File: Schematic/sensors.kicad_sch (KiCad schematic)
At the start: 19 parts, among them IC4 ICM-42688-P, IC5 MPU-6500, U4 QMC5883L, U5 SPL06-001

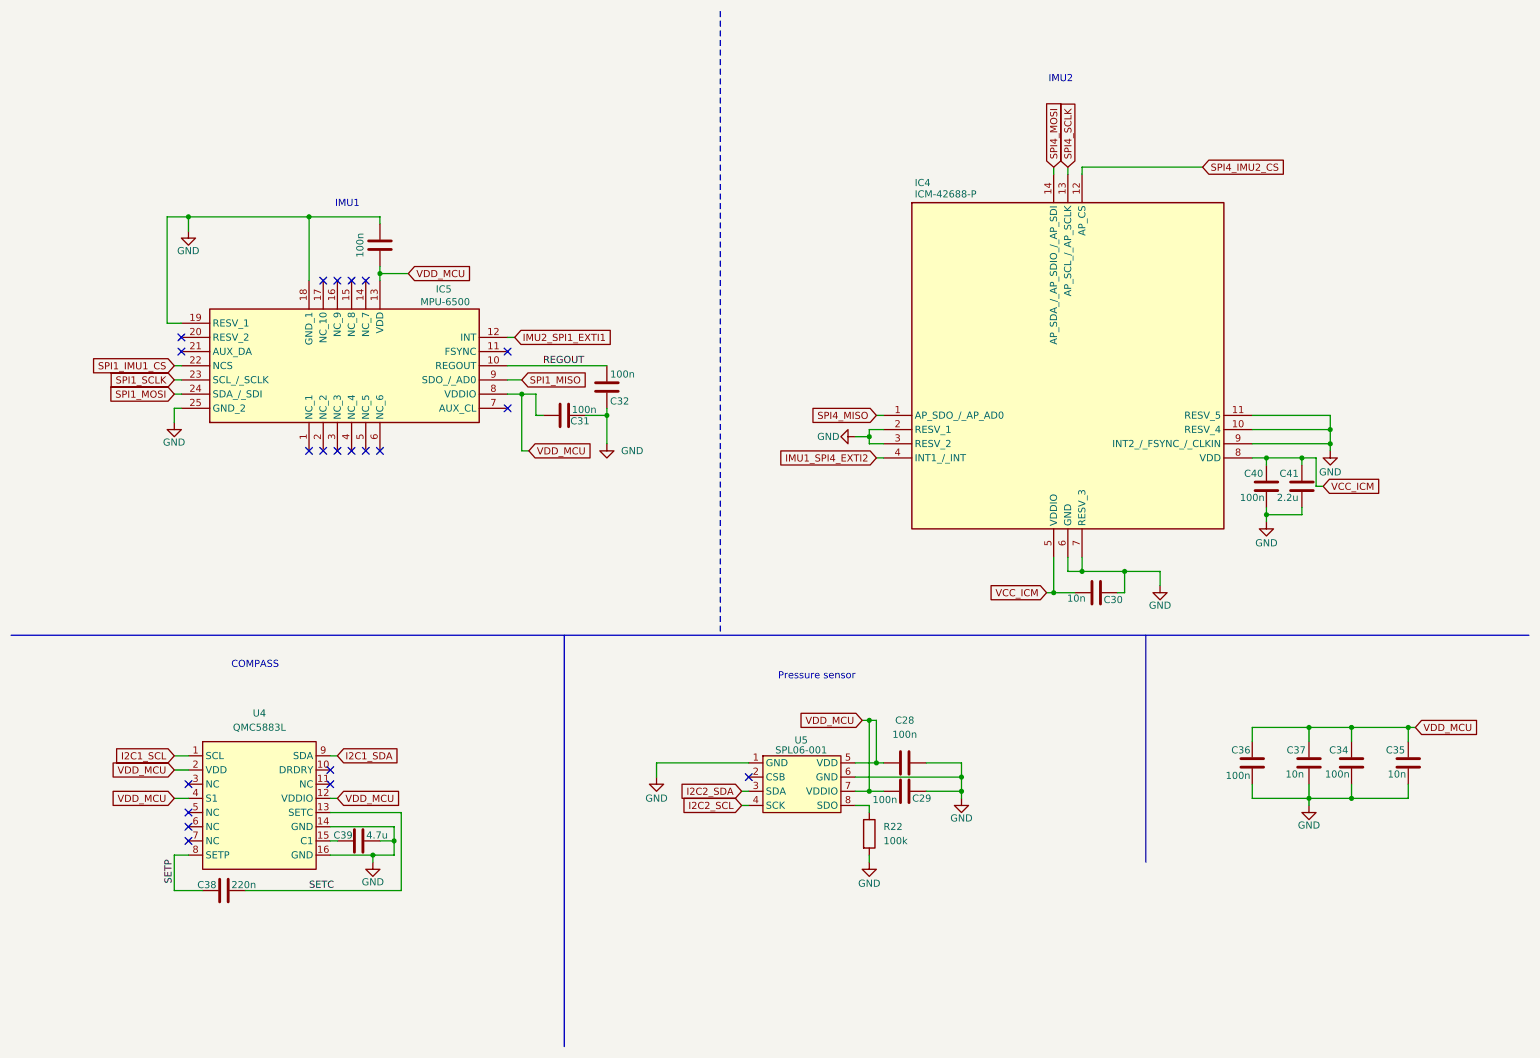
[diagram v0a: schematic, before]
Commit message: update: refine component labels for IMU and Magnetometer in schematic
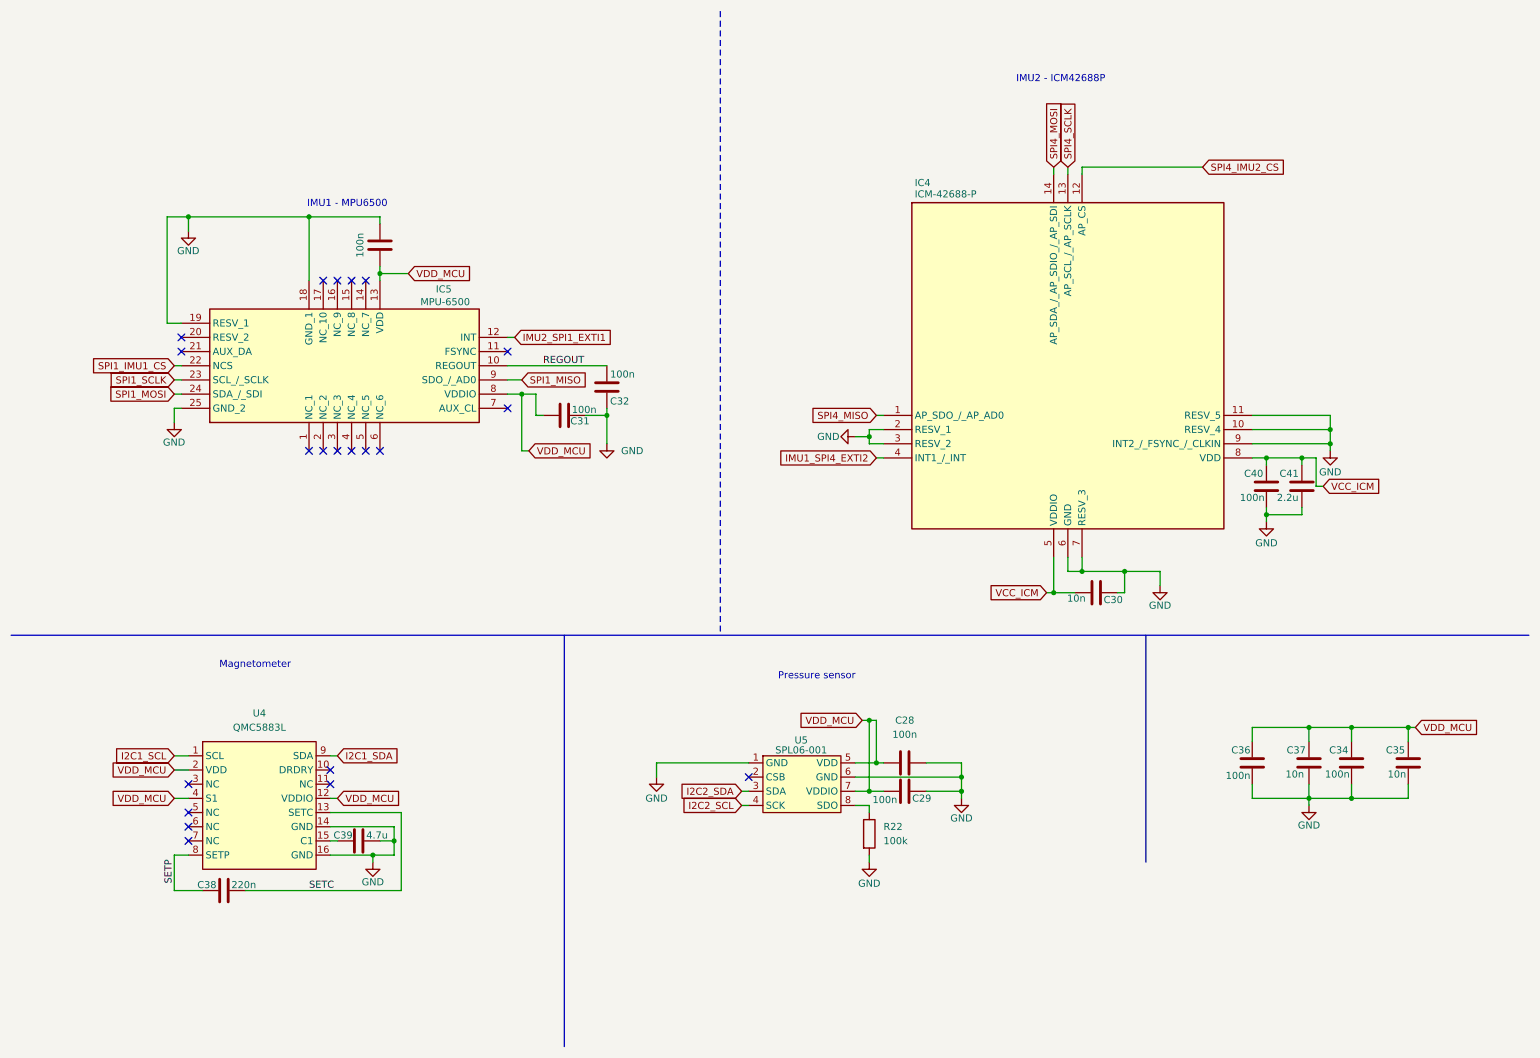
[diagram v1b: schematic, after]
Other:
- note added: "IMU1 - MPU6500"
- note added: "IMU2 - ICM42688P"
- note added: "Magnetometer"
- note removed: "COMPASS"
- note removed: "IMU1"
- note removed: "IMU2"
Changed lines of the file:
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@@
 	(generator_version "9.0")
 	(paper "A4")
-	(text "IMU2\n"
+	(text "IMU2 - ICM42688P\n"
 		(exclude_from_sim no)
 		(at 200.66 24.892 0)
@@
 		)
 	)
-	(text "IMU1\n"
+	(text "IMU1 - MPU6500\n"
 		(exclude_from_sim no)
 		(at 72.898 47.244 0)
@@
 		)
 	)
-	(text "COMPASS\n"
+	(text "Magnetometer\n"
 		(exclude_from_sim no)
 		(at 56.388 129.794 0)

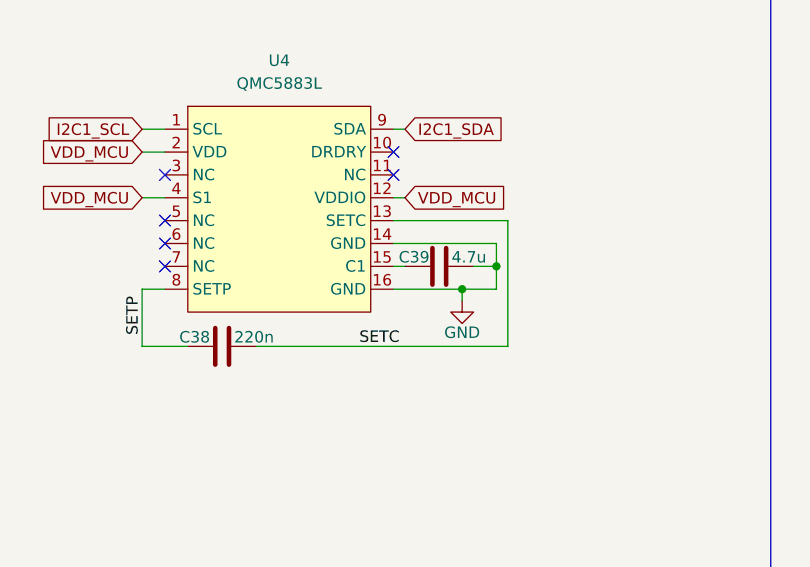
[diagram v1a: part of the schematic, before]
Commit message: Fix junction and wire positions in schematic; update capacitor and ground symbol properties
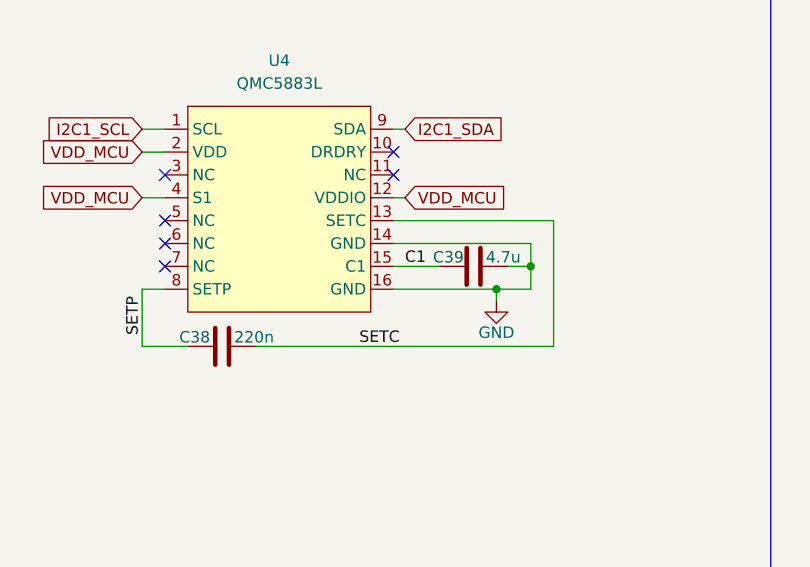
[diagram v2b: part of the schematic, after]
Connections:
- net C1: now reaches C39.1, U4.15 (C1)
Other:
- moved on the sheet: C39
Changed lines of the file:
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@@
 	)
 	(junction
-		(at 77.47 163.83)
+		(at 81.28 163.83)
 		(diameter 0)
 		(color 0 0 0 0)
@@
 	)
 	(junction
-		(at 81.28 161.29)
+		(at 85.09 161.29)
 		(diameter 0)
 		(color 0 0 0 0)
@@
 	(wire
 		(pts
-			(xy 69.85 161.29) (xy 71.12 161.29)
+			(xy 69.85 161.29) (xy 74.93 161.29)
 		)
 		(stroke
@@
 	(wire
 		(pts
-			(xy 77.47 163.83) (xy 77.47 165.1)
+			(xy 81.28 163.83) (xy 81.28 165.1)
 		)
 		(stroke
@@
 	(wire
 		(pts
-			(xy 78.74 161.29) (xy 81.28 161.29)
+			(xy 82.55 161.29) (xy 85.09 161.29)
 		)
 		(stroke
@@
 	(wire
 		(pts
-			(xy 77.47 163.83) (xy 81.28 163.83)
+			(xy 81.28 163.83) (xy 85.09 163.83)
 		)
 		(stroke
@@
 	(wire
 		(pts
-			(xy 82.55 170.18) (xy 82.55 156.21)
+			(xy 87.63 170.18) (xy 87.63 156.21)
 		)
 		(stroke
@@
 	(wire
 		(pts
-			(xy 69.85 158.75) (xy 81.28 158.75)
+			(xy 69.85 158.75) (xy 85.09 158.75)
 		)
 		(stroke
@@
 	(wire
 		(pts
-			(xy 69.85 156.21) (xy 82.55 156.21)
+			(xy 69.85 156.21) (xy 87.63 156.21)
 		)
 		(stroke
@@
 	(wire
 		(pts
-			(xy 69.85 163.83) (xy 77.47 163.83)
+			(xy 69.85 163.83) (xy 81.28 163.83)
 		)
 		(stroke
@@
 	(wire
 		(pts
-			(xy 54.61 170.18) (xy 82.55 170.18)
+			(xy 54.61 170.18) (xy 87.63 170.18)
 		)
 		(stroke
@@
 	(wire
 		(pts
-			(xy 81.28 158.75) (xy 81.28 161.29)
+			(xy 85.09 158.75) (xy 85.09 161.29)
 		)
 		(stroke
@@
 	(wire
 		(pts
-			(xy 81.28 161.29) (xy 81.28 163.83)
+			(xy 85.09 161.29) (xy 85.09 163.83)
 		)
 		(stroke
@@
 		)
 	)
+	(label "C1"
+		(at 71.12 161.29 0)
+		(effects
+			(font
+				(size 1.27 1.27)
+			)
+			(justify left bottom)
+		)
+	)
 	(label "SETC"
 		(at 66.04 170.18 0)
@@
 	(symbol
 		(lib_id "Device:C")
-		(at 74.93 161.29 90)
+		(at 78.74 161.29 90)
 		(unit 1)
 		(exclude_from_sim no)
@@
 		(dnp no)
 		(property "Reference" "C39"
-			(at 72.136 160.274 90)
+			(at 75.946 160.274 90)
 			(effects
 				(font
@@
 		)
 		(property "Value" "4.7u"
-			(at 78.232 160.274 90)
+			(at 82.042 160.274 90)
 			(effects
 				(font
@@
 		)
 		(property "Footprint" "Capacitor_SMD:C_0402_1005Metric"
-			(at 78.74 160.3248 0)
+			(at 82.55 160.3248 0)
 			(effects
 				(font
@@
 		)
 		(property "Datasheet" "https://www.samsungsem.com/resources/file/global/support/product_catalog/MLCC.pdf"
-			(at 74.93 161.29 0)
+			(at 78.74 161.29 0)
 			(effects
 				(font
@@
 		)
 		(property "Description" "Unpolarized capacitor"
-			(at 74.93 161.29 0)
+			(at 78.74 161.29 0)
 			(effects
 				(font
@@
 		)
 		(property "Fréquence" ""
-			(at 74.93 161.29 90)
+			(at 78.74 161.29 90)
 			(effects
 				(font
@@
 		)
 		(property "MPN" "CL10B105KO8NNNC"
-			(at 74.93 161.29 90)
+			(at 78.74 161.29 90)
 			(effects
 				(font
@@
 		)
 		(property "Manufacturer" "SAMSUNG"
-			(at 74.93 161.29 90)
+			(at 78.74 161.29 90)
 			(effects
 				(font
@@
 	(symbol
 		(lib_id "power:GND")
-		(at 77.47 165.1 0)
+		(at 81.28 165.1 0)
 		(unit 1)
 		(exclude_from_sim no)
@@
 		(dnp no)
 		(property "Reference" "#PWR032"
-			(at 77.47 171.45 0)
+			(at 81.28 171.45 0)
 			(effects
 				(font
@@
 		)
 		(property "Value" "GND"
-			(at 77.47 168.656 0)
+			(at 81.28 168.656 0)
 			(effects
 				(font
@@
 		)
 		(property "Footprint" ""
-			(at 77.47 165.1 0)
+			(at 81.28 165.1 0)
 			(effects
 				(font
@@
 		)
 		(property "Datasheet" ""
-			(at 77.47 165.1 0)
+			(at 81.28 165.1 0)
 			(effects
 				(font
@@
 		)
 		(property "Description" "Power symbol creates a global label with name \"GND\" , ground"
-			(at 77.47 165.1 0)
+			(at 81.28 165.1 0)
 			(effects
 				(font
